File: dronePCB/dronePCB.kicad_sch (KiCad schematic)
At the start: 27 parts, among them IC3 DPS368XTSA1, IC4 ICM-42688-P, J6 RunCam Split 4, J7 VID_ANT, U7 E28-2G4M12SX, U8 AT7456E, U9 TX5823, Y2 27MHz

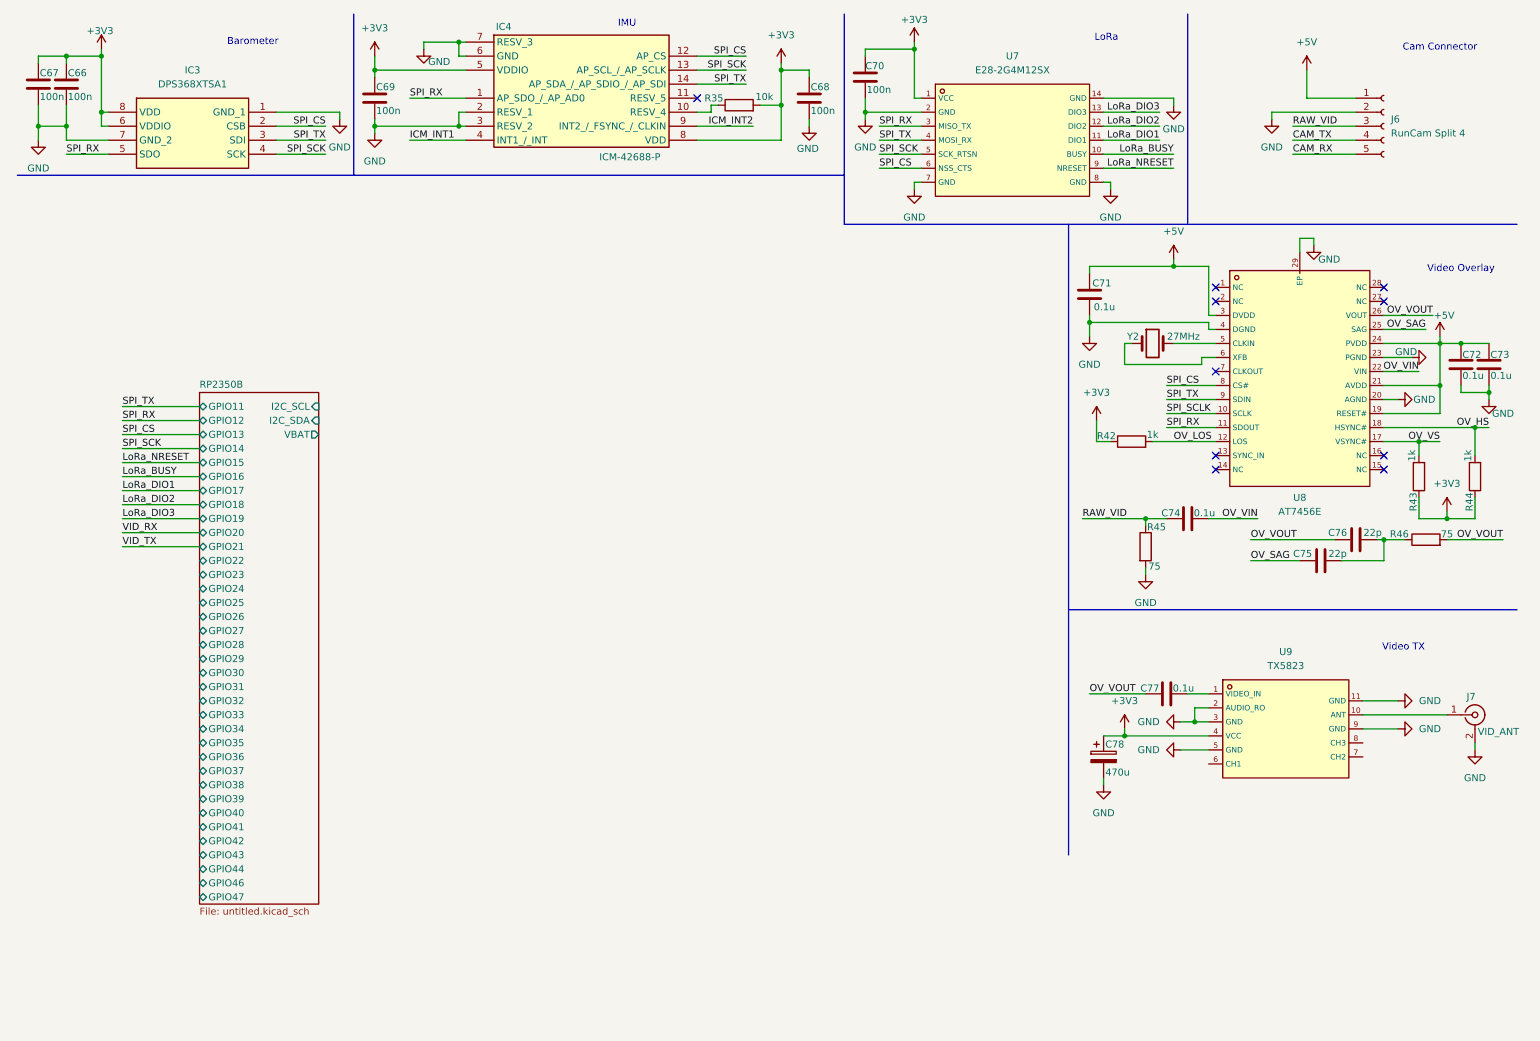
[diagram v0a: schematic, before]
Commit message: Added micro sd card slot
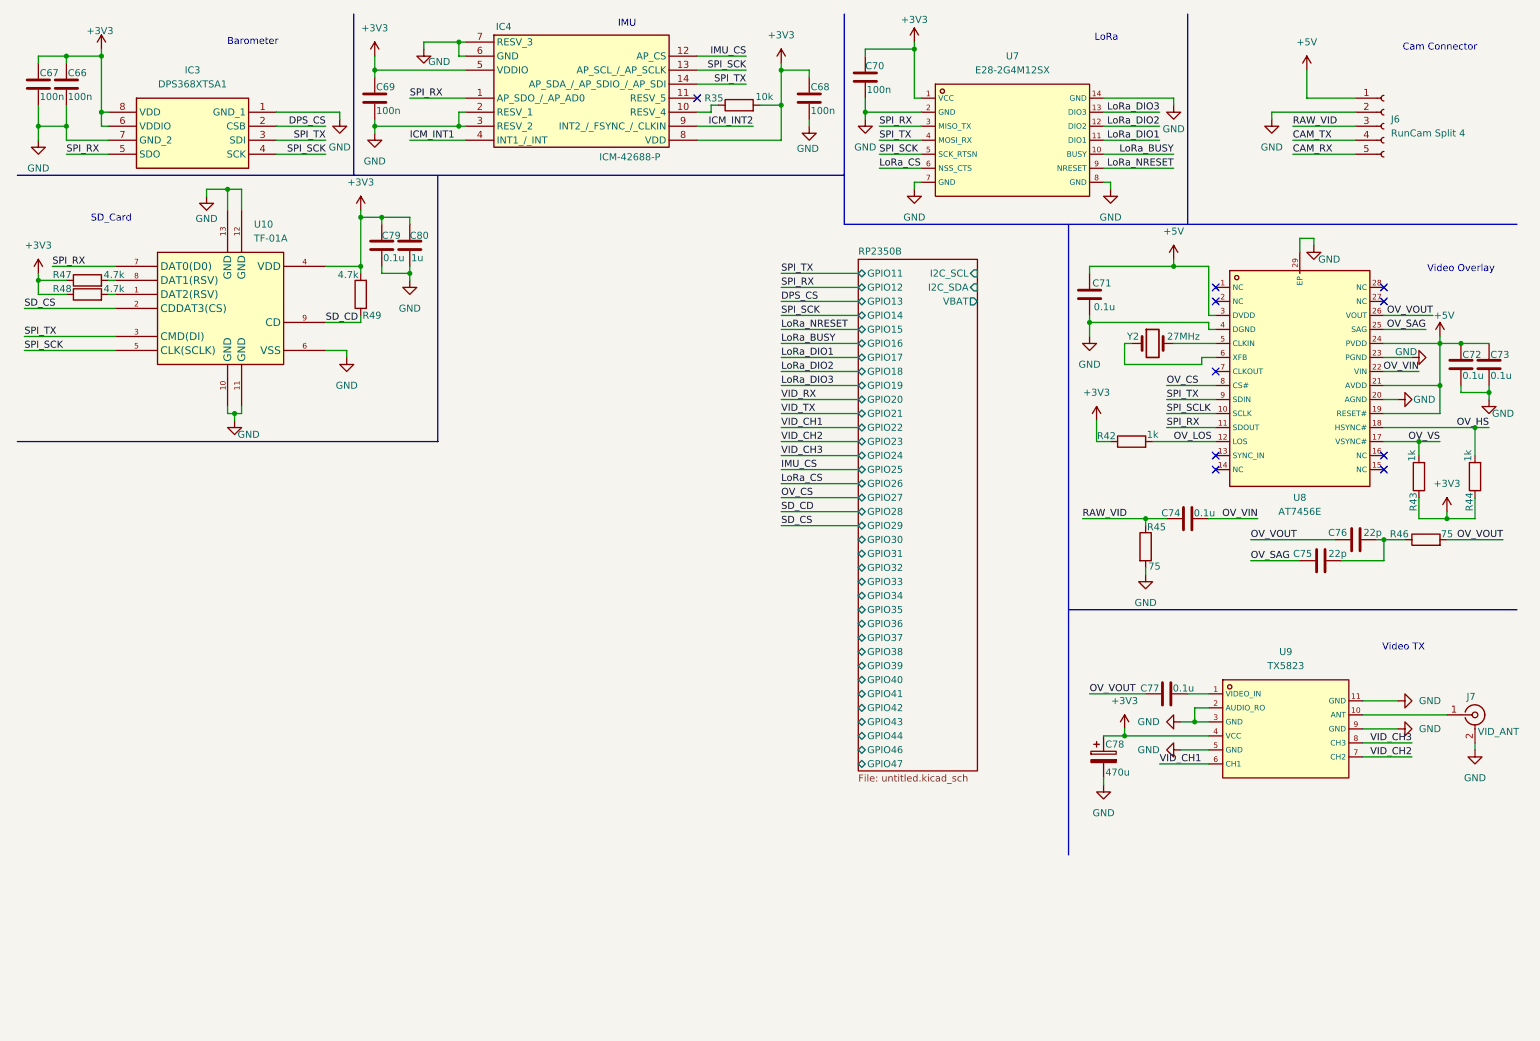
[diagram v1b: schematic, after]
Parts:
- added C79: 0.1u, symbol Device:C
- added C80: 1u, symbol Device:C
- added R47, R48, R49: 4.7k, symbol Device:R
- added U10: TF-01A, footprint:TF-SMD_TF-01A, symbol TF-01A:TF-01A
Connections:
- net +3V3: now also C79.1, C80.1, R47.1, R48.1, R49.2, U10.4 (VDD)
- net GND: now also C79.2, C80.2, U10.10 (GND), U10.11 (GND), U10.12 (GND), U10.13 (GND), U10.6 (VSS)
- net SPI_RX: now also U10.7 (DAT0(D0))
- net SPI_SCK: now also U10.5 (CLK(SCLK))
- net SPI_TX: now also U10.3 (CMD(DI))
- net VID_CH1: now reaches U9.6 (CH1)
- net VID_CH2: now reaches U9.7 (CH2)
- net VID_CH3: now reaches U9.8 (CH3)
- removed net SPI_CS: IC3.2 (CSB), IC4.12 (AP_CS), U7.6 (NSS_CTS), U8.8 (CS#)
- new net: R48.2, U10.1 (DAT2(RSV))
- new net: R47.2, U10.8 (DAT1(RSV))
- new net DPS_CS: IC3.2 (CSB)
- new net IMU_CS: IC4.12 (AP_CS)
- new net LoRa_CS: U7.6 (NSS_CTS)
- new net OV_CS: U8.8 (CS#)
- new net SD_CD: R49.1, U10.9 (CD)
- new net SD_CS: U10.2 (CDDAT3(CS))
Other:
- note added: "SD_Card"

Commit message: Added micro SD, GPS, magnetometer, gimbal, DVR, Strobes and ToF sensors
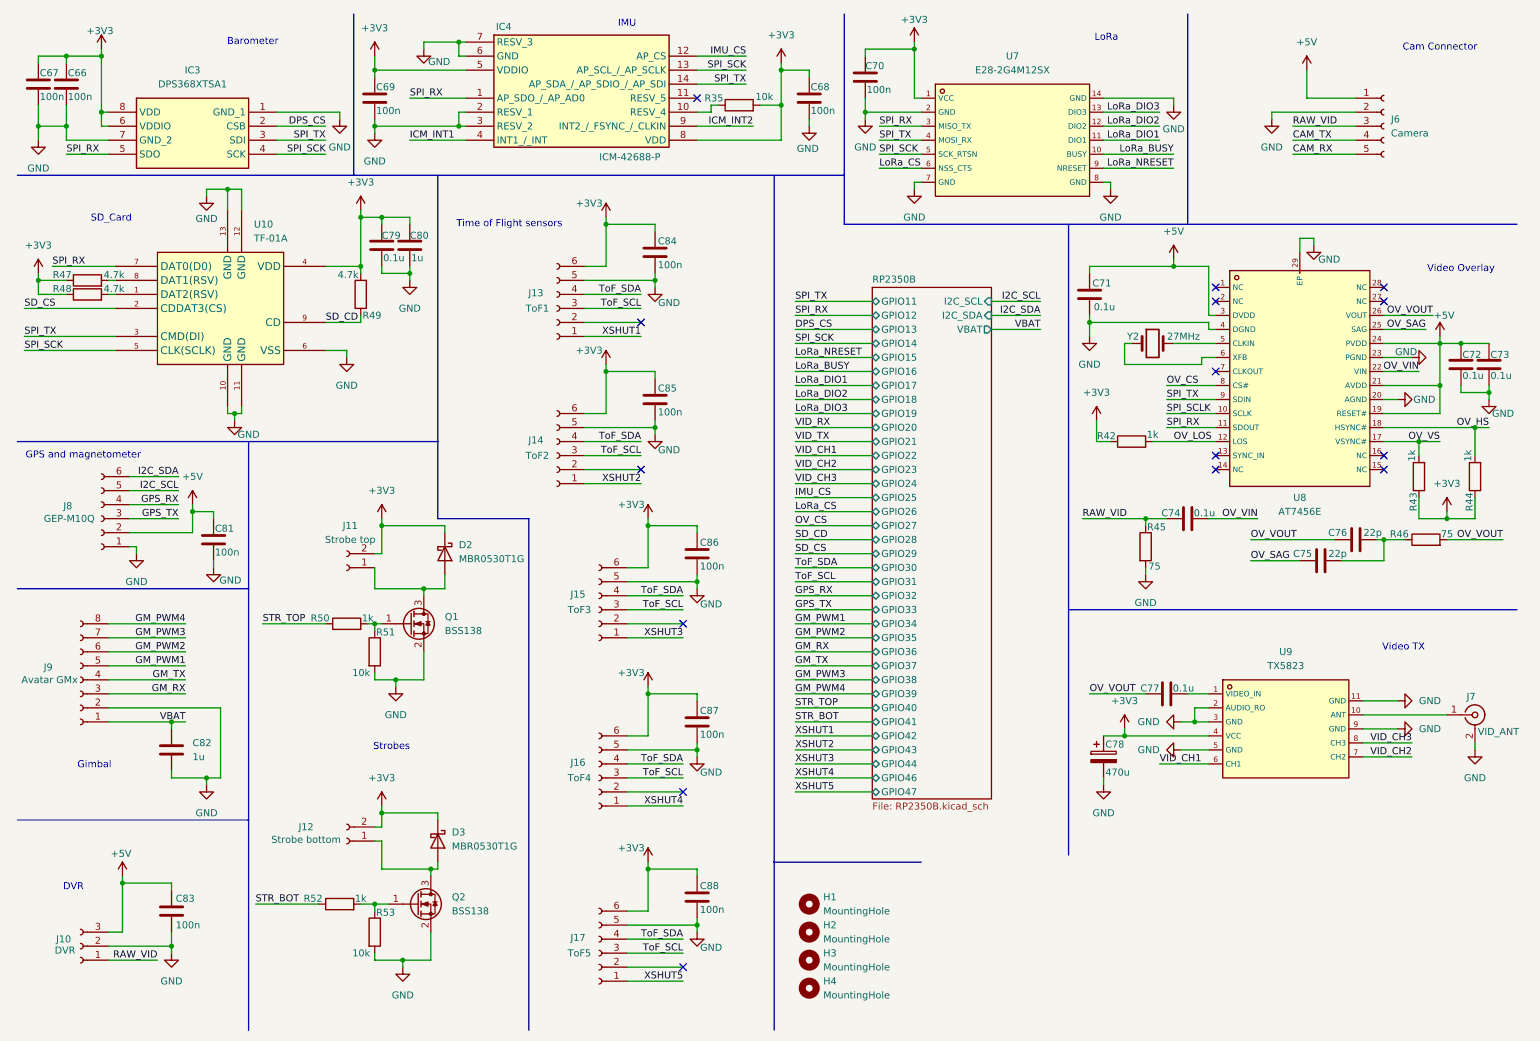
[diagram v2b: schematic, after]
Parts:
- added C81, C83, C84, C85, C86, C87, C88: 100n, symbol Device:C
- added C82: 1u, symbol Device:C
- added D2, D3: MBR0530T1G, Diode_SMD:D_SOD-123, symbol Diode:MBR0530
- added H1, H2, H3, H4: MountingHole, symbol Mechanical:MountingHole
- added J10: DVR, symbol Connector:Conn_01x03_Socket
- added J11: Strobe top, symbol Connector:Conn_01x02_Socket
- added J12: Strobe bottom, symbol Connector:Conn_01x02_Socket
- added J13: ToF1, symbol Connector:Conn_01x06_Socket
- added J14: ToF2, symbol Connector:Conn_01x06_Socket
- added J15: ToF3, symbol Connector:Conn_01x06_Socket
- added J16: ToF4, symbol Connector:Conn_01x06_Socket
- added J17: ToF5, symbol Connector:Conn_01x06_Socket
- added J8: GEP-M10Q, symbol Connector:Conn_01x06_Socket
- added J9: Avatar GMx, symbol Connector:Conn_01x08_Socket
- added Q1, Q2: BSS138, Package_TO_SOT_SMD:SOT-23, symbol Transistor_FET:BSS138
- added R50, R52: 1k, symbol Device:R
- added R51, R53: 10k, symbol Device:R
- J6: value RunCam Split 4 -> Camera
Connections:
- net +3V3: now also C84.1, C85.1, C86.1, C87.1, C88.1, D2.1 (K), D3.1 (K), J11.2 (Pin_2), J12.2 (Pin_2), J13.6 (Pin_6), J14.6 (Pin_6), J15.6 (Pin_6), J16.6 (Pin_6), J17.6 (Pin_6)
- net +5V: now also C81.1, C83.1, J10.3 (Pin_3), J8.2 (Pin_2)
- net GND: now also C81.2, C82.2, C83.2, C84.2, C85.2, C86.2, C87.2, C88.2, J10.2 (Pin_2), J13.5 (Pin_5), J14.5 (Pin_5), J15.5 (Pin_5), J16.5 (Pin_5), J17.5 (Pin_5), J8.1 (Pin_1), J9.2 (Pin_2), Q1.2 (S), Q2.2 (S), R51.2, R53.2
- net RAW_VID: now also J10.1 (Pin_1)
- new net: D3.2 (A), J12.1 (Pin_1), Q2.3 (D)
- new net: Q2.1 (G), R52.2, R53.1
- new net: D2.2 (A), J11.1 (Pin_1), Q1.3 (D)
- new net: Q1.1 (G), R50.2, R51.1
- new net GM_PWM1: J9.5 (Pin_5)
- new net GM_PWM2: J9.6 (Pin_6)
- new net GM_PWM3: J9.7 (Pin_7)
- new net GM_PWM4: J9.8 (Pin_8)
- new net GM_RX: J9.3 (Pin_3)
- new net GM_TX: J9.4 (Pin_4)
- new net GPS_RX: J8.4 (Pin_4)
- new net GPS_TX: J8.3 (Pin_3)
- new net I2C_SCL: J8.5 (Pin_5)
- new net I2C_SDA: J8.6 (Pin_6)
- new net STR_BOT: R52.1
- new net STR_TOP: R50.1
- new net ToF_SCL: J13.3 (Pin_3), J14.3 (Pin_3), J15.3 (Pin_3), J16.3 (Pin_3), J17.3 (Pin_3)
- new net ToF_SDA: J13.4 (Pin_4), J14.4 (Pin_4), J15.4 (Pin_4), J16.4 (Pin_4), J17.4 (Pin_4)
- new net VBAT: C82.1, J9.1 (Pin_1)
- new net XSHUT1: J13.1 (Pin_1)
- new net XSHUT2: J14.1 (Pin_1)
- new net XSHUT3: J15.1 (Pin_1)
- new net XSHUT4: J16.1 (Pin_1)
- new net XSHUT5: J17.1 (Pin_1)
- no-connect marks 10 -> 15
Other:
- sheet RP2350B: file untitled.kicad_sch -> RP2350B.kicad_sch
- note added: "DVR"
- note added: "GPS and magnetometer"
- note added: "Gimbal"
- note added: "Strobes"
- note added: "Time of Flight sensors"
- company: (none) -> Author: Mejpek
- title: (none) -> Main Board

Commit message: Added strobe PCB
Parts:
- C71, C72, C73, C74, C77, C79: value 0.1u -> 100n
- J13: value ToF1 -> ToF400C
- J14: value ToF2 -> ToF400C
- J15: value ToF3 -> ToF400C
- J16: value ToF4 -> ToF400C
- J17: value ToF5 -> ToF400C
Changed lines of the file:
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@@
 		(dnp no)
 		(property "Reference" "J17"
-			(at 114.3 180.086 0)
+			(at 113.792 180.086 0)
 			(effects
 				(font
@@
 			)
 		)
-		(property "Value" "ToF5"
-			(at 114.554 182.88 0)
+		(property "Value" "ToF400C"
+			(at 113.538 182.88 0)
 			(effects
 				(font
@@
 		(dnp no)
 		(property "Reference" "J13"
-			(at 106.68 63.246 0)
+			(at 106.172 63.246 0)
 			(effects
 				(font
@@
 			)
 		)
-		(property "Value" "ToF1"
-			(at 106.934 66.04 0)
+		(property "Value" "ToF400C"
+			(at 106.172 66.294 0)
 			(effects
 				(font
@@
 			)
 		)
-		(property "Value" "0.1u"
+		(property "Value" "100n"
 			(at 274.574 78.232 0)
 			(effects
@@
 			)
 		)
-		(property "Value" "0.1u"
+		(property "Value" "100n"
 			(at 78.994 56.896 0)
 			(effects
@@
 		(dnp no)
 		(property "Reference" "J15"
-			(at 114.3 117.856 0)
+			(at 113.792 117.856 0)
 			(effects
 				(font
@@
 			)
 		)
-		(property "Value" "ToF3"
-			(at 114.554 120.65 0)
+		(property "Value" "ToF400C"
+			(at 113.538 120.904 0)
 			(effects
 				(font
@@
 			)
 		)
-		(property "Value" "0.1u"
-			(at 224.028 134.874 90)
+		(property "Value" "100n"
+			(at 224.79 134.62 90)
 			(effects
 				(font
@@
 			)
 		)
-		(property "Value" "0.1u"
-			(at 227.838 103.124 90)
+		(property "Value" "100n"
+			(at 228.346 103.124 90)
 			(effects
 				(font
@@
 		(dnp no)
 		(property "Reference" "J14"
-			(at 106.68 89.916 0)
+			(at 105.664 89.662 0)
 			(effects
 				(font
@@
 			)
 		)
-		(property "Value" "ToF2"
-			(at 106.934 92.71 0)
+		(property "Value" "ToF400C"
+			(at 105.664 92.71 0)
 			(effects
 				(font
@@
 			)
 		)
-		(property "Value" "0.1u"
+		(property "Value" "100n"
 			(at 279.654 78.232 0)
 			(effects
@@
 		(dnp no)
 		(property "Reference" "J16"
-			(at 114.3 148.336 0)
+			(at 113.792 148.336 0)
 			(effects
 				(font
@@
 			)
 		)
-		(property "Value" "ToF4"
-			(at 114.554 151.13 0)
+		(property "Value" "ToF400C"
+			(at 113.792 151.13 0)
 			(effects
 				(font
@@
 			)
 		)
-		(property "Value" "0.1u"
+		(property "Value" "100n"
 			(at 207.772 65.786 0)
 			(effects
